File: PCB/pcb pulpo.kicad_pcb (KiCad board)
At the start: 2 copper layers, 70 parts, among them J1 fan1, J10 fan8, J11 fan8, J12 izq, J13 dcha, J14 inf, J2 Entrada 12V, J3 fan2, J4 fan3, J5 fan4, J6 fan5, J7 fan6, J8 fan7, J9 fan8, Q1 IRF540N, Q10 IRF540N, Q2 IRF540N, Q3 IRF540N, Q4 IRF540N, Q5 IRF540N, Q6 IRF540N, Q7 IRF540N, Q8 IRF540N, Q9 IRF540N, U1 Teensy3.0, U2 LM7805_TO220

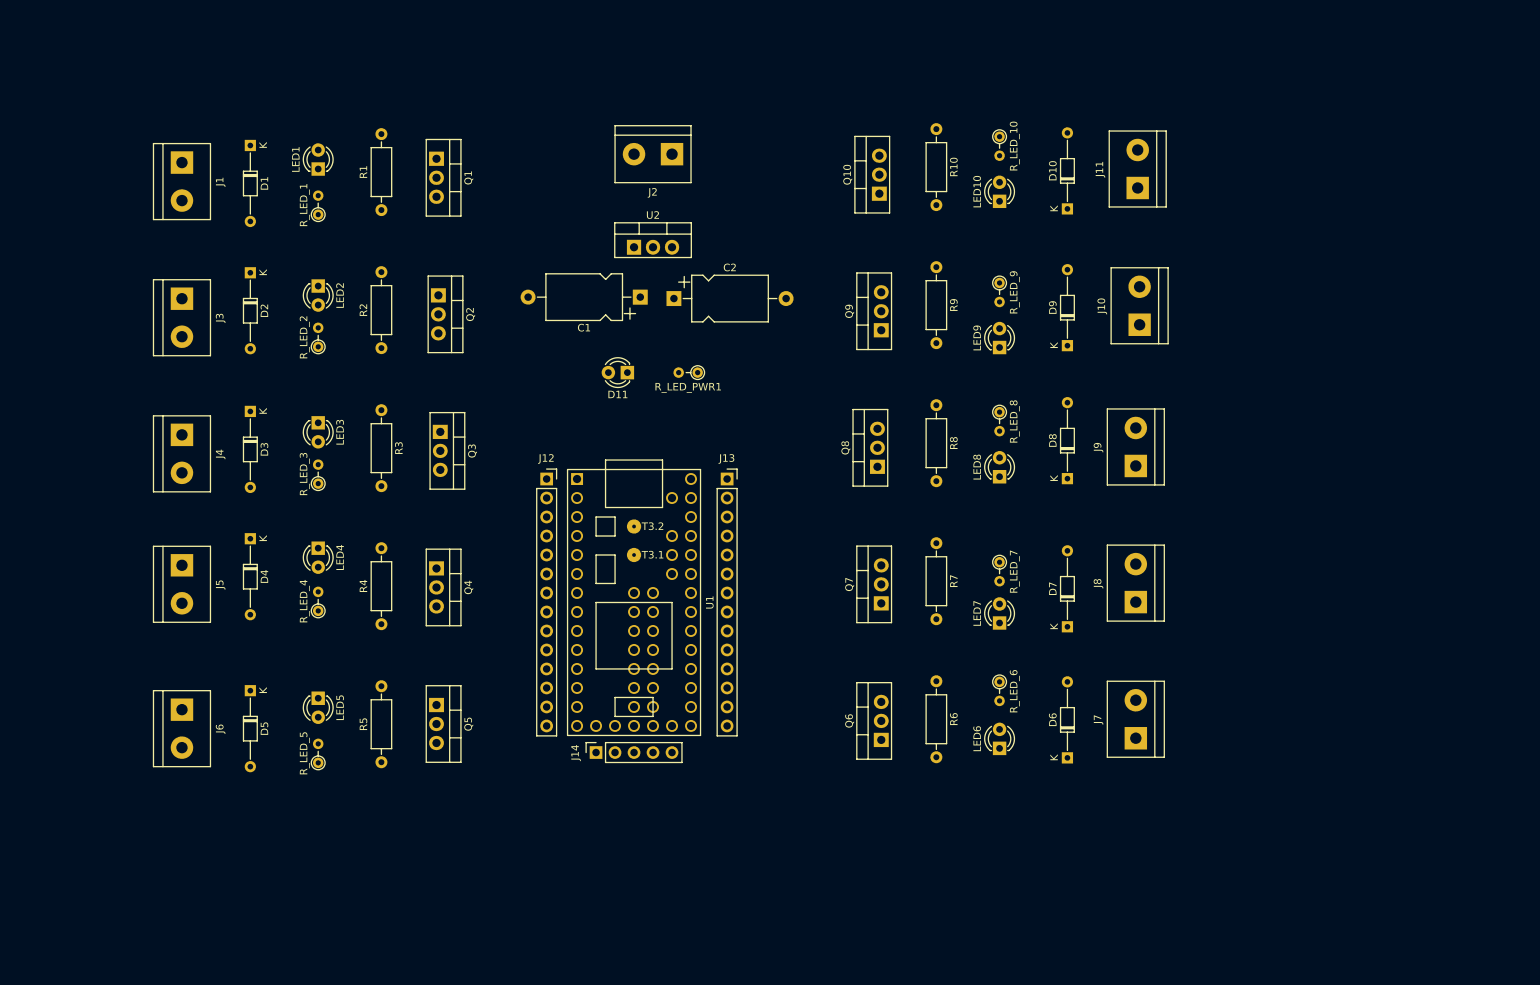
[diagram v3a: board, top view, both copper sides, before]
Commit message: mejoras en componentes
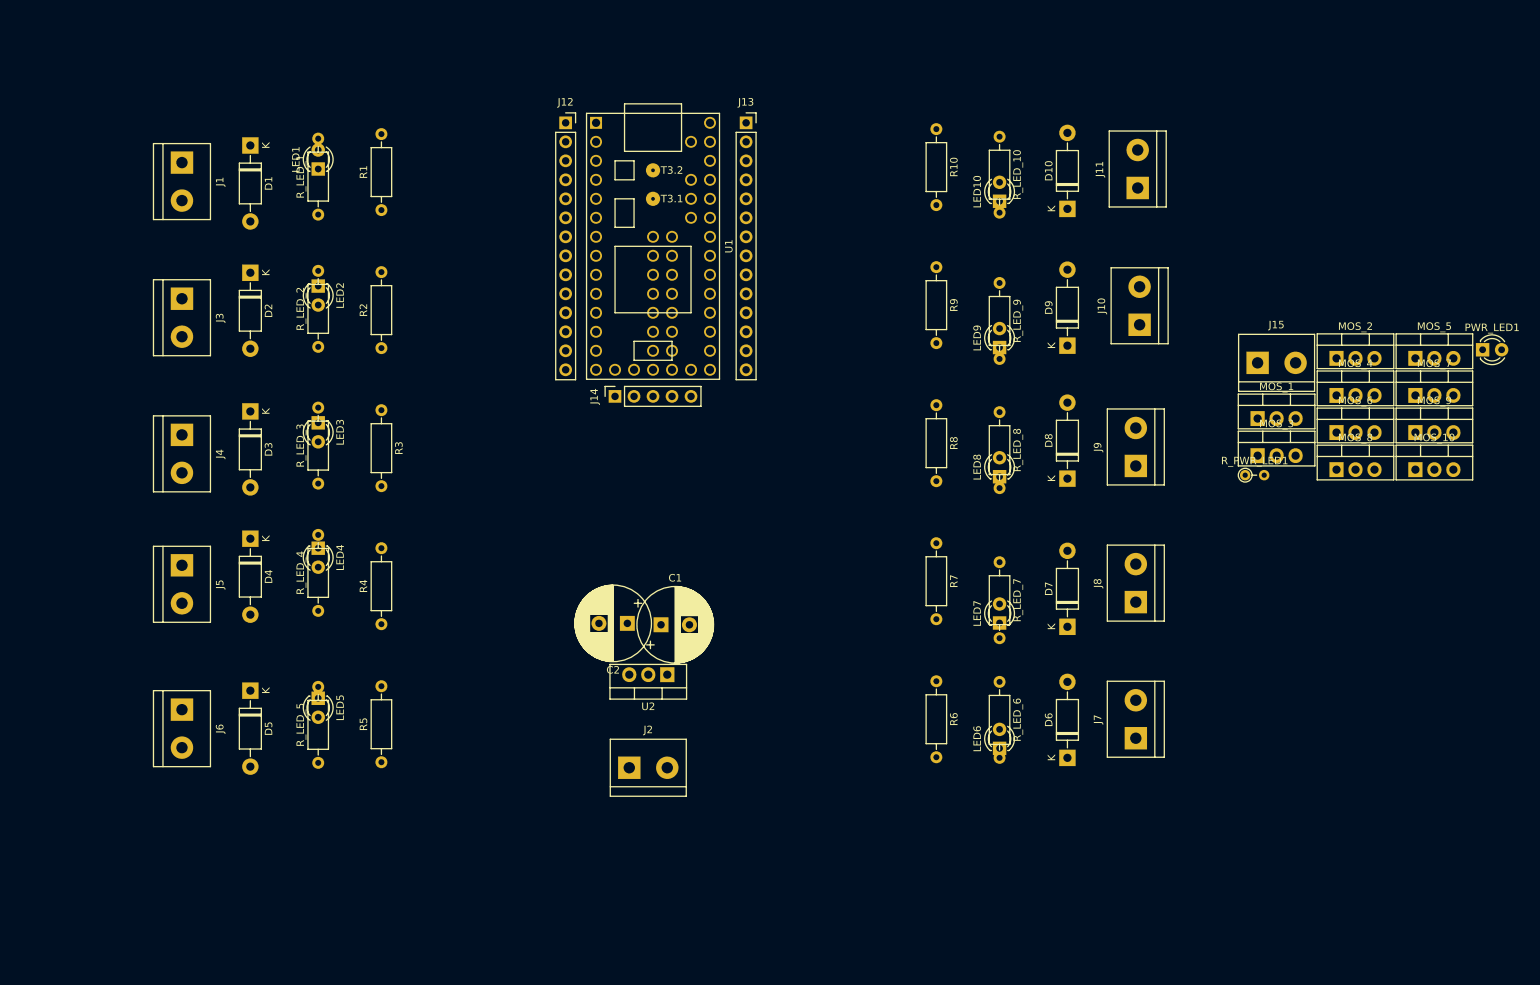
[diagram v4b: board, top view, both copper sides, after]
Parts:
- removed D11: LED, LED_THT:LED_D3.0mm
- removed Q1, Q10, Q2, Q3, Q4, Q5, Q6, Q7, Q8, Q9: IRF540N, Package_TO_SOT_THT:TO-220-3_Vertical
- removed R_LED_PWR1: R_Small, Resistor_THT:R_Axial_DIN0204_L3.6mm_D1.6mm_P2.54mm_Vertical
- added J15: Entrada 12V, TerminalBlock:TerminalBlock_bornier-2_P5.08mm, F.Cu at (169.7, 61.2)
- added MOS_1: RFP50N06, Package_TO_SOT_THT:TO-220-3_Vertical, F.Cu at (169.7, 68.6)
- added MOS_10: RFP50N06, Package_TO_SOT_THT:TO-220-3_Vertical, F.Cu at (190.8, 75.5)
- added MOS_2: RFP50N06, Package_TO_SOT_THT:TO-220-3_Vertical, F.Cu at (180.3, 60.6)
- added MOS_3: RFP50N06, Package_TO_SOT_THT:TO-220-3_Vertical, F.Cu at (169.7, 73.6)
- added MOS_4: RFP50N06, Package_TO_SOT_THT:TO-220-3_Vertical, F.Cu at (180.3, 65.5)
- added MOS_5: RFP50N06, Package_TO_SOT_THT:TO-220-3_Vertical, F.Cu at (190.8, 60.6)
- added MOS_6: RFP50N06, Package_TO_SOT_THT:TO-220-3_Vertical, F.Cu at (180.3, 70.5)
- added MOS_7: RFP50N06, Package_TO_SOT_THT:TO-220-3_Vertical, F.Cu at (190.8, 65.5)
- added MOS_8: RFP50N06, Package_TO_SOT_THT:TO-220-3_Vertical, F.Cu at (180.3, 75.5)
- added MOS_9: RFP50N06, Package_TO_SOT_THT:TO-220-3_Vertical, F.Cu at (190.8, 70.5)
- added PWR_LED1: LED, LED_THT:LED_D3.0mm, F.Cu at (199.8, 59.4)
- added R_PWR_LED1: R_Small, Resistor_THT:R_Axial_DIN0204_L3.6mm_D1.6mm_P2.54mm_Vertical, F.Cu at (168.1, 76.2)
- C1, C2: footprint Capacitor_THT:CP_Axial_L10.0mm_D6.0mm_P15.00mm_Horizontal -> Capacitor_THT:CP_Radial_D10.0mm_P3.80mm
- D1, D10, D2, D3, D4, D5, D6, D7, D8, D9: value DIODE -> 1N4004; footprint Diode_THT:D_DO-34_SOD68_P10.16mm_Horizontal -> Diode_THT:D_DO-41_SOD81_P10.16mm_Horizontal
- J10: value fan8 -> fan9
- J11: value fan8 -> fan10
- J2: value Entrada 12V -> fan2
- J3: value fan2 -> fan3
- J4: value fan3 -> fan4
- J5: value fan4 -> fan5
- J6: value fan5 -> direct output
- R1, R10, R2, R3, R4, R5, R6, R7, R8, R9: value R -> 10K
- R_LED_1, R_LED_10, R_LED_2, R_LED_3, R_LED_4, R_LED_5, R_LED_6, R_LED_7, R_LED_8, R_LED_9: value R_LED -> 330R; footprint Resistor_THT:R_Axial_DIN0204_L3.6mm_D1.6mm_P2.54mm_Vertical -> Resistor_THT:R_Axial_DIN0207_L6.3mm_D2.5mm_P10.16mm_Horizontal
- moved J2 82.2 mm to (85.7, 115.3), turned to 0 degrees
- moved U2 57.3 mm to (90.8, 102.9), turned to 180 degrees
- moved J12 47.7 mm to (77.2, 29.1)
- moved J13 47.7 mm to (101.3, 29.1)
- moved J14 47.7 mm to (83.8, 65.7)
- moved U1 47.7 mm to (88.9, 45.6)
- moved C1 43.9 mm to (90.0, 96.2), turned to 0 degrees
- moved C2 43.9 mm to (85.5, 96.0), turned to 180 degrees
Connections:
- D1 pad 1: Net-(D1-Pad1) -> +12V
- D1 pad 2: +12V -> Net-(D1-Pad2)
- D10 pad 1: Net-(D10-Pad1) -> +12V
- D10 pad 2: +12V -> Net-(D10-Pad2)
- D2 pad 1: Net-(D2-Pad1) -> +12V
- D2 pad 2: +12V -> Net-(D2-Pad2)
- D3 pad 1: Net-(D3-Pad1) -> +12V
- D3 pad 2: +12V -> Net-(D3-Pad2)
- D4 pad 1: Net-(D4-Pad1) -> +12V
- D4 pad 2: +12V -> Net-(D4-Pad2)
- D5 pad 1: Net-(D5-Pad1) -> +12V
- D5 pad 2: +12V -> Net-(D5-Pad2)
- D6 pad 1: Net-(D6-Pad1) -> +12V
- D6 pad 2: +12V -> Net-(D6-Pad2)
- D7 pad 1: Net-(D7-Pad1) -> +12V
- D7 pad 2: +12V -> Net-(D7-Pad2)
- D8 pad 1: Net-(D8-Pad1) -> +12V
- D8 pad 2: +12V -> Net-(D8-Pad2)
- D9 pad 1: Net-(D9-Pad1) -> +12V
- D9 pad 2: +12V -> Net-(D9-Pad2)
- J1 pad 1: Net-(D1-Pad1) -> +12V
- J1 pad 2: +12V -> Net-(D1-Pad2)
- J10 pad 1: Net-(D9-Pad1) -> +12V
- J10 pad 2: +12V -> Net-(D9-Pad2)
- J11 pad 1: Net-(D10-Pad1) -> +12V
- J11 pad 2: +12V -> Net-(D10-Pad2)
- J2 pad 1: GND -> +12V
- J2 pad 2: +12V -> Net-(D2-Pad2)
- J3 pad 1: Net-(D2-Pad1) -> +12V
- J3 pad 2: +12V -> Net-(D3-Pad2)
- J4 pad 1: Net-(D3-Pad1) -> +12V
- J4 pad 2: +12V -> Net-(D4-Pad2)
- J5 pad 1: Net-(D4-Pad1) -> +12V
- J5 pad 2: +12V -> Net-(D5-Pad2)
- J6 pad 1: Net-(D5-Pad1) -> +12V
- J6 pad 2: +12V -> GND
- J7 pad 1: Net-(D6-Pad1) -> +12V
- J7 pad 2: +12V -> Net-(D6-Pad2)
- J8 pad 1: Net-(D7-Pad1) -> +12V
- J8 pad 2: +12V -> Net-(D7-Pad2)
- J9 pad 1: Net-(D8-Pad1) -> +12V
- J9 pad 2: +12V -> Net-(D8-Pad2)
- LED1 pad 1: Net-(D1-Pad1) -> GND
- LED10 pad 1: Net-(D10-Pad1) -> GND
- LED2 pad 1: Net-(D2-Pad1) -> GND
- LED3 pad 1: Net-(D3-Pad1) -> GND
- LED4 pad 1: Net-(D4-Pad1) -> GND
- LED5 pad 1: Net-(D5-Pad1) -> GND
- LED6 pad 1: Net-(D6-Pad1) -> GND
- LED7 pad 1: Net-(D7-Pad1) -> GND
- LED8 pad 1: Net-(D8-Pad1) -> GND
- LED9 pad 1: Net-(D9-Pad1) -> GND
- R1 pad 1: GND -> pin1
- R1 pad 2: pin1 -> GND
- R10 pad 1: GND -> pin10
- R10 pad 2: pin10 -> GND
- R2 pad 1: GND -> pin2
- R2 pad 2: pin2 -> GND
- R3 pad 1: GND -> pin3
- R3 pad 2: pin3 -> GND
- R4 pad 1: GND -> pin4
- R4 pad 2: pin4 -> GND
- R5 pad 1: GND -> pin5
- R5 pad 2: pin5 -> GND
- R6 pad 1: GND -> pin6
- R6 pad 2: pin6 -> GND
- R7 pad 1: GND -> pin7
- R7 pad 2: pin7 -> GND
- R8 pad 1: GND -> pin8
- R8 pad 2: pin8 -> GND
- R9 pad 1: GND -> pin9
- R9 pad 2: pin9 -> GND
- R_LED_1 pad 1: +12V -> pin1
- R_LED_10 pad 1: +12V -> pin10
- R_LED_2 pad 1: +12V -> pin2
- R_LED_3 pad 1: +12V -> pin3
- R_LED_4 pad 1: +12V -> pin4
- R_LED_5 pad 1: +12V -> pin5
- R_LED_6 pad 1: +12V -> pin6
- R_LED_7 pad 1: +12V -> pin7
- R_LED_8 pad 1: +12V -> pin8
- R_LED_9 pad 1: +12V -> pin9
- U1 pad 34: Net-(U1-Pad34) -> (no net)
- U1 pad 35: Net-(U1-Pad35) -> (no net)
- U1 pad 36: Net-(U1-Pad36) -> (no net)
- U1 pad 37: Net-(U1-Pad37) -> (no net)
- U1 pad 38: Net-(U1-Pad38) -> (no net)
- U1 pad 40: Net-(U1-Pad40) -> (no net)
- U1 pad 41: Net-(U1-Pad41) -> (no net)
- U1 pad 42: Net-(U1-Pad42) -> (no net)
- U1 pad 43: Net-(U1-Pad43) -> (no net)
- U1 pad 44: Net-(U1-Pad44) -> (no net)
- U1 pad 45: Net-(U1-Pad45) -> (no net)
- U1 pad 46: Net-(U1-Pad46) -> (no net)
- U1 pad 47: Net-(U1-Pad47) -> (no net)
- U1 pad 48: Net-(U1-Pad48) -> (no net)
- U1 pad 49: Net-(U1-Pad49) -> (no net)
- U1 pad 50: Net-(U1-Pad50) -> (no net)
- U1 pad 51: Net-(U1-Pad51) -> (no net)

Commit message: cambios en la pcb. añadido footprint conector Pablo. Falta cambiar algunos componentes y routear
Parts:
- C1, C2: footprint Capacitor_THT:CP_Radial_D10.0mm_P3.80mm -> Capacitor_THT:CP_Radial_D6.3mm_P2.50mm
- J15: footprint TerminalBlock:TerminalBlock_bornier-2_P5.08mm -> teensy:conector pablo pulpo hinchoshwi
- moved J15 25.5 mm to (183.4, 39.6)
- moved R1 1.30 mm to (52.5, 42.0)
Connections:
- U1 pad 34: (no net) -> Net-(U1-Pad34)
- U1 pad 35: (no net) -> Net-(U1-Pad35)
- U1 pad 36: (no net) -> Net-(U1-Pad36)
- U1 pad 37: (no net) -> Net-(U1-Pad37)
- U1 pad 38: (no net) -> Net-(U1-Pad38)
- U1 pad 40: (no net) -> Net-(U1-Pad40)
- U1 pad 41: (no net) -> Net-(U1-Pad41)
- U1 pad 42: (no net) -> Net-(U1-Pad42)
- U1 pad 43: (no net) -> Net-(U1-Pad43)
- U1 pad 44: (no net) -> Net-(U1-Pad44)
- U1 pad 45: (no net) -> Net-(U1-Pad45)
- U1 pad 46: (no net) -> Net-(U1-Pad46)
- U1 pad 47: (no net) -> Net-(U1-Pad47)
- U1 pad 48: (no net) -> Net-(U1-Pad48)
- U1 pad 49: (no net) -> Net-(U1-Pad49)
- U1 pad 50: (no net) -> Net-(U1-Pad50)
- U1 pad 51: (no net) -> Net-(U1-Pad51)

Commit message: Esquema y PCB en versión release 1
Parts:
- removed J15: Entrada 12V, teensy:conector pablo pulpo hinchoshwi
- removed PWR_LED1: LED, LED_THT:LED_D3.0mm
- removed R1, R10, R2, R3, R4, R5, R7: 10K, Resistor_THT:R_Axial_DIN0207_L6.3mm_D2.5mm_P10.16mm_Horizontal
- removed R_LED_1, R_LED_10, R_LED_2, R_LED_3, R_LED_4, R_LED_5, R_LED_7: 330R, Resistor_THT:R_Axial_DIN0207_L6.3mm_D2.5mm_P10.16mm_Horizontal
- added 10K: 10K, Resistor_THT:R_Axial_DIN0207_L6.3mm_D2.5mm_P10.16mm_Horizontal, F.Cu at (113.0, 43.2)
- added 10K: 10K, Resistor_THT:R_Axial_DIN0207_L6.3mm_D2.5mm_P10.16mm_Horizontal, F.Cu at (162.6, 120.7)
- added 10K: 10K, Resistor_THT:R_Axial_DIN0207_L6.3mm_D2.5mm_P10.16mm_Horizontal, F.Cu at (113.0, 62.9)
- added 10K: 10K, Resistor_THT:R_Axial_DIN0207_L6.3mm_D2.5mm_P10.16mm_Horizontal, F.Cu at (113.0, 82.5)
- added 10K: 10K, Resistor_THT:R_Axial_DIN0207_L6.3mm_D2.5mm_P10.16mm_Horizontal, F.Cu at (113.0, 101.6)
- added 10K: 10K, Resistor_THT:R_Axial_DIN0207_L6.3mm_D2.5mm_P10.16mm_Horizontal, F.Cu at (113.0, 120.7)
- added 10K: 10K, Resistor_THT:R_Axial_DIN0207_L6.3mm_D2.5mm_P10.16mm_Horizontal, F.Cu at (162.6, 62.9)
- added 330R: 330R, Resistor_THT:R_Axial_DIN0207_L6.3mm_D2.5mm_P10.16mm_Horizontal, F.Cu at (108.6, 43.2)
- added 330R: 330R, Resistor_THT:R_Axial_DIN0207_L6.3mm_D2.5mm_P10.16mm_Horizontal, F.Cu at (167.0, 120.7)
- added 330R: 330R, Resistor_THT:R_Axial_DIN0207_L6.3mm_D2.5mm_P10.16mm_Horizontal, F.Cu at (108.6, 62.9)
- added 330R: 330R, Resistor_THT:R_Axial_DIN0207_L6.3mm_D2.5mm_P10.16mm_Horizontal, F.Cu at (108.6, 82.5)
- added 330R: 330R, Resistor_THT:R_Axial_DIN0207_L6.3mm_D2.5mm_P10.16mm_Horizontal, F.Cu at (108.6, 101.6)
- added 330R: 330R, Resistor_THT:R_Axial_DIN0207_L6.3mm_D2.5mm_P10.16mm_Horizontal, F.Cu at (108.6, 120.7)
- added 330R: 330R, Resistor_THT:R_Axial_DIN0207_L6.3mm_D2.5mm_P10.16mm_Horizontal, F.Cu at (167.0, 62.9)
- added G***: LOGO, Logos:oshwi35x45, B.Cu at (135.9, 101.0)
- added Input 12VDC: Entrada 12V, teensy:conector pablo pulpo hinchoshwi, F.Cu at (137.8, 135.3)
- added PWR: LED, LED_THT:LED_D3.0mm, F.Cu at (128.9, 100.3)
- added REF**: MountingHole_3.2mm_M3, MountingHole:MountingHole_3.2mm_M3, F.Cu at (190.8, 136.8)
- added REF**: MountingHole_3.2mm_M3, MountingHole:MountingHole_3.2mm_M3, F.Cu at (190.8, 38.5)
- added REF**: MountingHole_3.2mm_M3, MountingHole:MountingHole_3.2mm_M3, F.Cu at (84.8, 38.5)
- added REF**: MountingHole_3.2mm_M3, MountingHole:MountingHole_3.2mm_M3, F.Cu at (84.8, 136.8)
- Direct output: renamed from J11; value fan10 -> Direct output
- J1: value fan1 -> Fan1
- J10: value fan9 -> Fan10
- J2: value fan2 -> Fan2
- J3: value fan3 -> Fan3
- J4: value fan4 -> Fan4
- J5: value fan5 -> Fan5
- J6: value direct output -> Fan6
- J7: value fan6 -> Fan7
- J8: value fan7 -> Fan8
- J9: value fan8 -> Fan9
- U1: value Teensy3.0 -> Teensy3.2
- moved J6 173.5 mm to (189.9, 50.8), turned to 90 degrees
- moved MOS_5 110.3 mm to (100.3, 123.6), turned to 270 degrees
- moved D10 98.2 mm to (181.6, 131.4)
- moved MOS_4 88.8 mm to (100.3, 104.1), turned to 270 degrees
- moved LED10 88.4 mm to (154.9, 125.7), turned to 0 degrees
- moved J10 81.2 mm to (189.9, 128.9)
- moved MOS_2 80.1 mm to (100.3, 65.4), turned to 270 degrees
- moved LED4 78.7 mm to (120.0, 106.7), turned to 180 degrees
- moved LED5 78.4 mm to (120.0, 125.7), turned to 180 degrees
- moved LED3 78.1 mm to (120.0, 87.6), turned to 180 degrees
- moved LED2 77.8 mm to (120.0, 67.9), turned to 180 degrees
- moved LED1 77.0 mm to (120.0, 48.3), turned to 180 degrees
- moved Direct output 76.2 mm to (135.3, 111.8), turned to 0 degrees
- moved MOS_1 73.1 mm to (100.3, 45.7), turned to 270 degrees
- moved D6 71.2 mm to (181.6, 53.3)
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- renumbered R6 to 10K, R8 to 10K, R9 to 10K, R_PWR_LED1 to 330R, R_LED_6 to 330R, R_LED_8 to 330R, R_LED_9 to 330R
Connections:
- 10K pad 1: pin8 -> pin9
- 10K pad 1: pin9 -> pin8
- 330R pad 1: pin8 -> pin9
- 330R pad 1: pin9 -> pin8
- Direct output pad 2: Net-(D10-Pad2) -> GND
- J10 pad 2: Net-(D9-Pad2) -> Net-(D10-Pad2)
- J6 pad 2: GND -> Net-(D6-Pad2)
- J7 pad 2: Net-(D6-Pad2) -> Net-(D7-Pad2)
- J8 pad 2: Net-(D7-Pad2) -> Net-(D8-Pad2)
- J9 pad 2: Net-(D8-Pad2) -> Net-(D9-Pad2)
- MOS_10 pad 1: pin10 -> pin7
- MOS_7 pad 1: pin7 -> pin10
- MOS_8 pad 1: pin8 -> pin9
- MOS_9 pad 1: pin9 -> pin8
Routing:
- net pin7: track 0.00 -> 89.0 mm
- net pin6: track 0.00 -> 84.0 mm
- net Net-(C2-Pad1): track 0.00 -> 80.9 mm
- net pin5: track 0.00 -> 74.9 mm
- net pin8: track 0.00 -> 73.4 mm
- net pin4: track 0.00 -> 65.6 mm
- net pin9: track 0.00 -> 55.7 mm
- net pin3: track 0.00 -> 46.8 mm
- net pin1: track 0.00 -> 39.2 mm
- net pin10: track 0.00 -> 38.6 mm
- net pin2: track 0.00 -> 33.3 mm
- net Net-(D9-Pad2): track 0.00 -> 18.0 mm
- net Net-(D5-Pad2): track 0.00 -> 18.0 mm
- net Net-(D8-Pad2): track 0.00 -> 17.8 mm
- net Net-(D10-Pad2): track 0.00 -> 17.8 mm
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- added copper zone on F.Cu, net +12V
- added copper zone on B.Cu, net GND
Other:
- board outline added: 116.8 x 109.2 mm
- net class Default: trace_width 0.25 -> 0.5
- rule pad_to_mask_clearance: 0.2 -> 0
- board text added: "+"
- board text added: "+ -"
- board text added: "-"
- board text added: "HinchOSHWi V1"
- board text added: "Iraisy C. - Milo B. - Pablo G."
